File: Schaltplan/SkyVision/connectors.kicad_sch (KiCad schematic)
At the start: 3 parts, among them J2 HBX, J3 DEC, J4 ST4

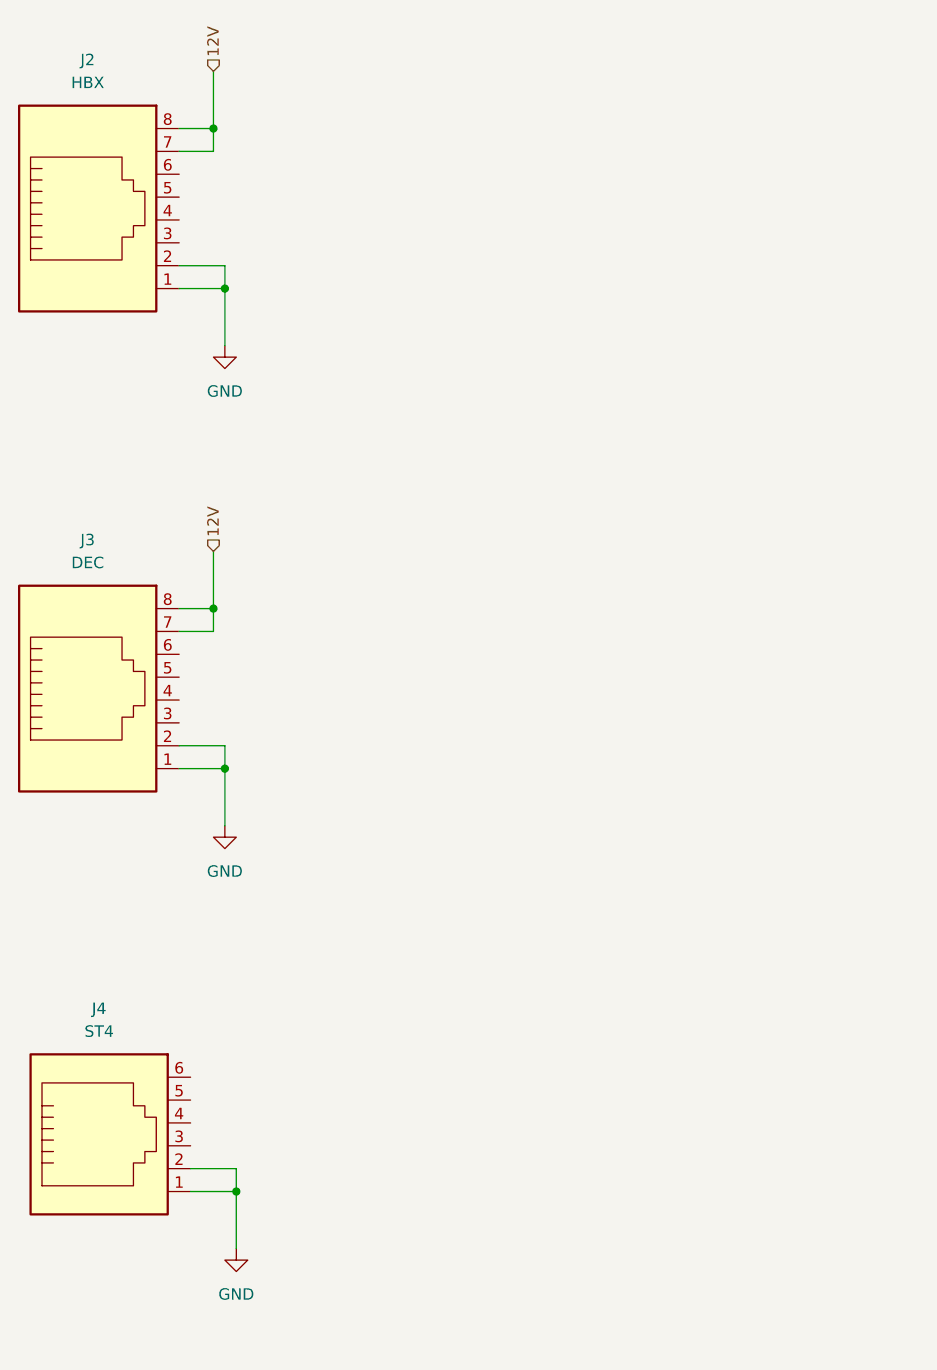
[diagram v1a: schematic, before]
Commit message: Schaltplan aufgeräumt
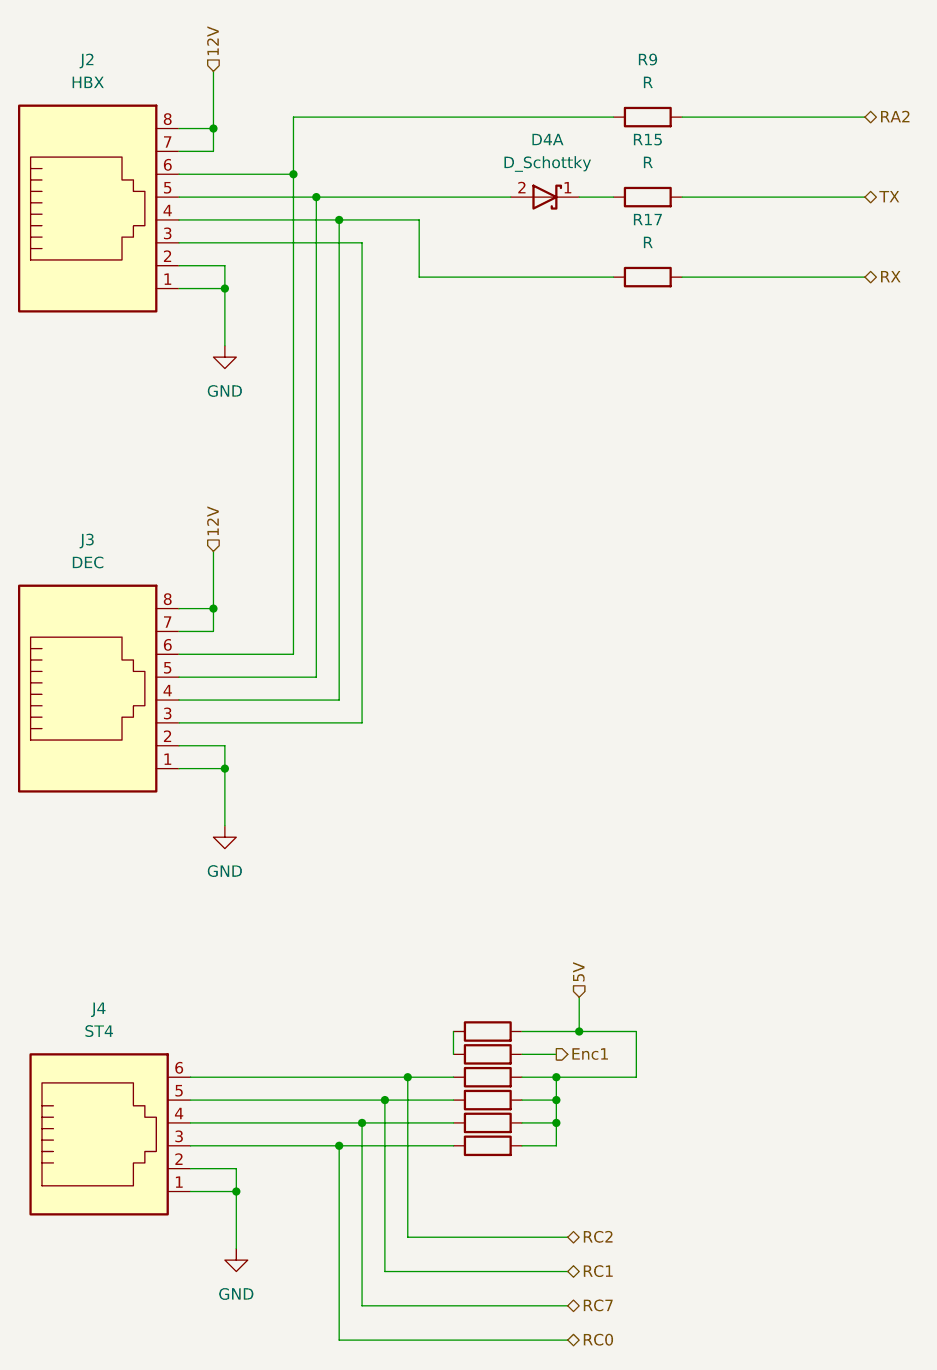
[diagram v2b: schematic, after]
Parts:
- added D4: D_Schottky, symbol Device:D_Schottky_Dual_CommonAnode_KAK_Split
- added R15 (x2), R17 (x2), R18, R22, R9 (x3): R, symbol Device:R
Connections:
- net at J3.3: now also J2.3
- net at J3.4: now also J2.4, R17.1
- net at J3.5: now also J2.5, D4.2 (A)
- net at J3.6: now also J2.6, R9.1
- net RC0: now reaches J4.3
- net RC0: now also R22.1
- net RC7: now reaches J4.4
- net RC7: now also R18.1
- net RC1: now reaches J4.5
- net RC1: now also R17.1
- net RC2: now reaches J4.6
- net RC2: now also R9.1
- new net: R15.1, R9.1
- new net: D4.1 (K), R15.1
- new net 5V: R17.2, R18.2, R22.2, R9.2, R9.2
- new net Enc1: R15.2
- new net RA2: R9.2
- new net RX: R17.2
- new net TX: R15.2

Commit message: MS Antwort log
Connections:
- net 12V: now also J2.1, J2.2, J3.1, J3.2; no longer J2.7, J2.8, J3.7, J3.8
- net GND: now also J2.7, J2.8, J3.7, J3.8; no longer J2.1, J2.2, J3.1, J3.2
- net RX: now also R15.2; no longer R17.2
- net TX: now also R17.2; no longer R15.2
- net at J2.4, J3.4: now also D4.2 (A); no longer R17.1
- net at J2.3, J3.3: now also R9.1
- net at J2.5, J3.5: now also R15.1; no longer D4.2 (A)
- net at J2.6, J3.6: no longer R9.1
- net at D4.1 (K): now also R17.1; no longer R15.1
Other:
- moved on the sheet: D4A, R15, R17, R9
